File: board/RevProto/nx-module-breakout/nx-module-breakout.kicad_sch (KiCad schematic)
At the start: 20 parts, among them J1 Conn_02x15_Odd_Even, J2 DF40C-60DS-0.4V(51), J3 Conn_02x15_Odd_Even, J4 Conn_02x15_Odd_Even, J5 DF40C-60DS-0.4V(51), J6 SFV22R-2STE1HLF, J7 SFV22R-2STE1HLF, J8 Conn_02x06_Odd_Even

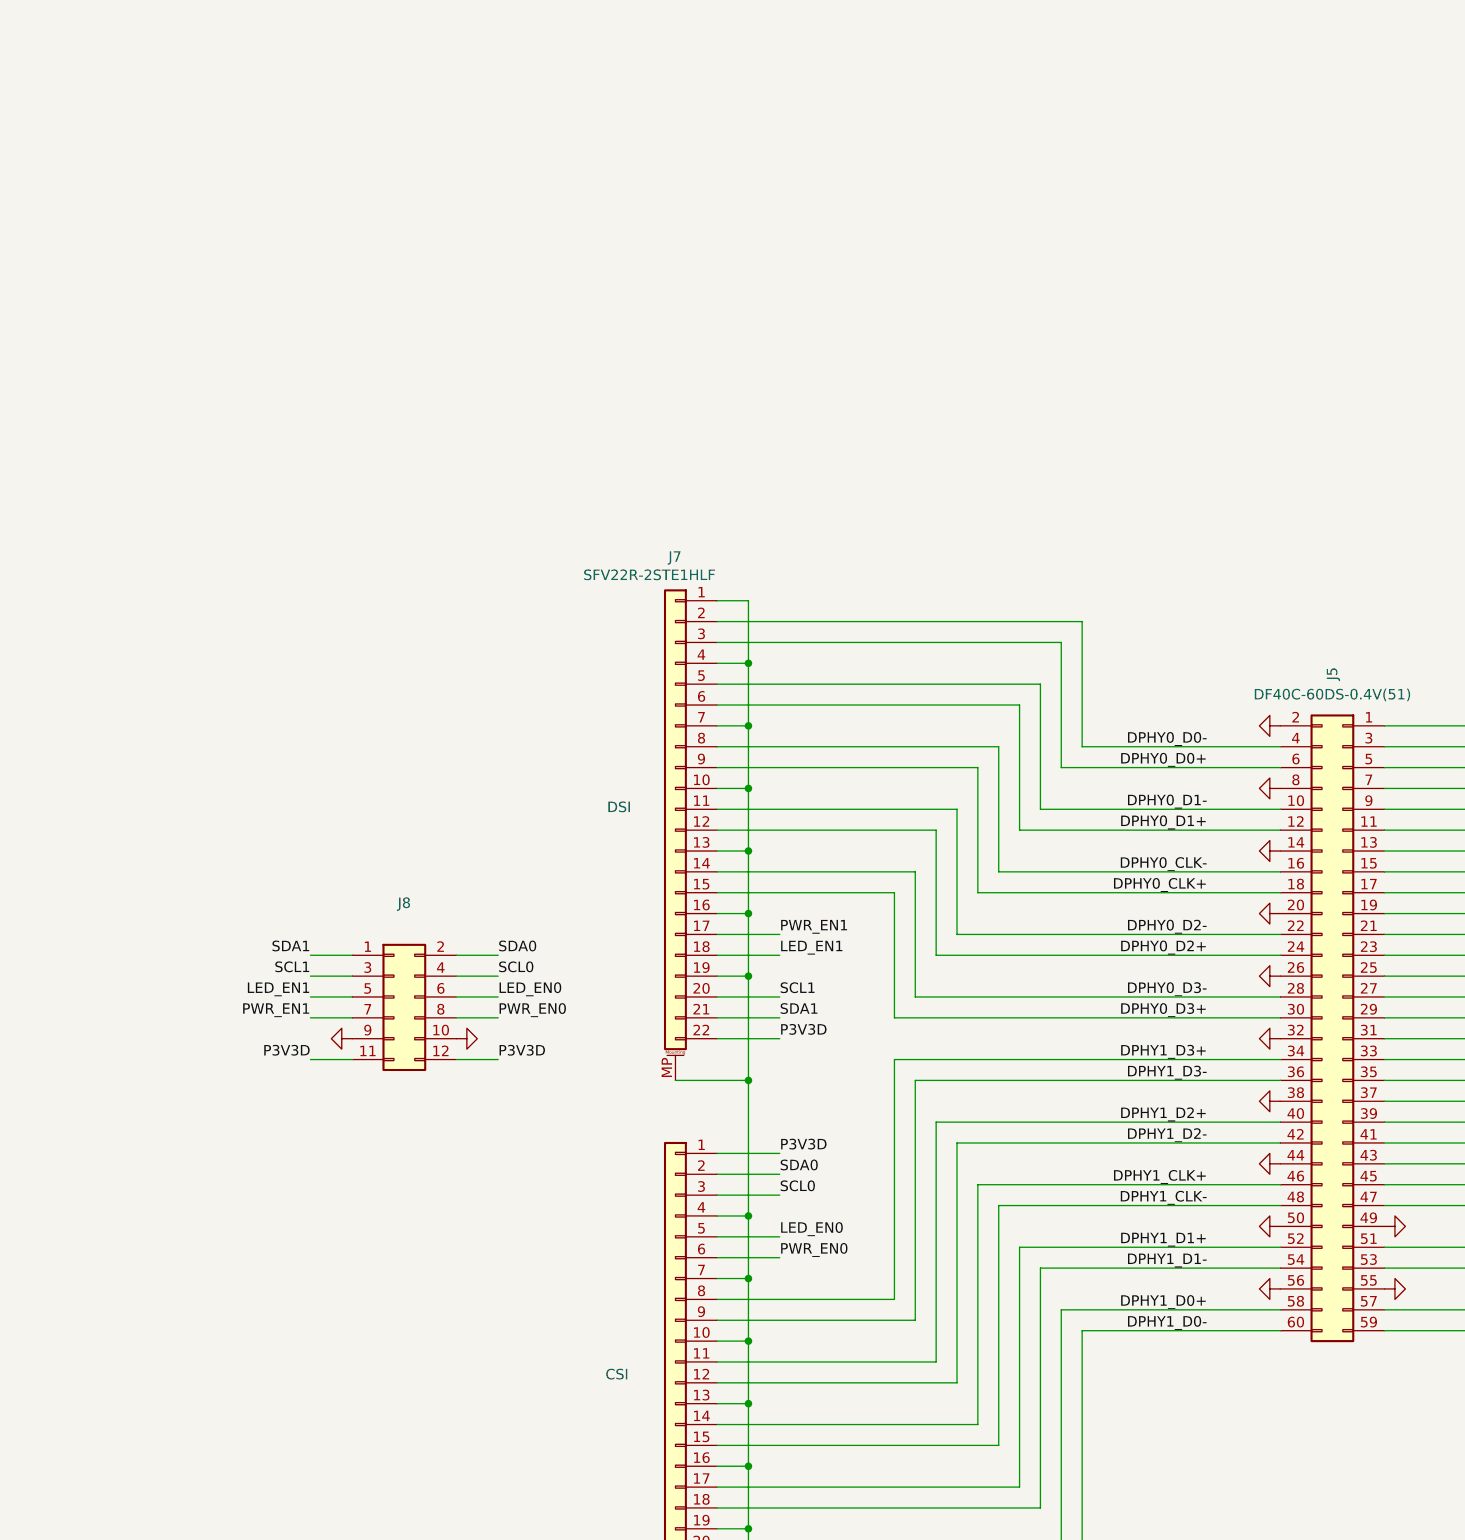
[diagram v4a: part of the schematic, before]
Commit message: Add USB connector, LDOs for power.
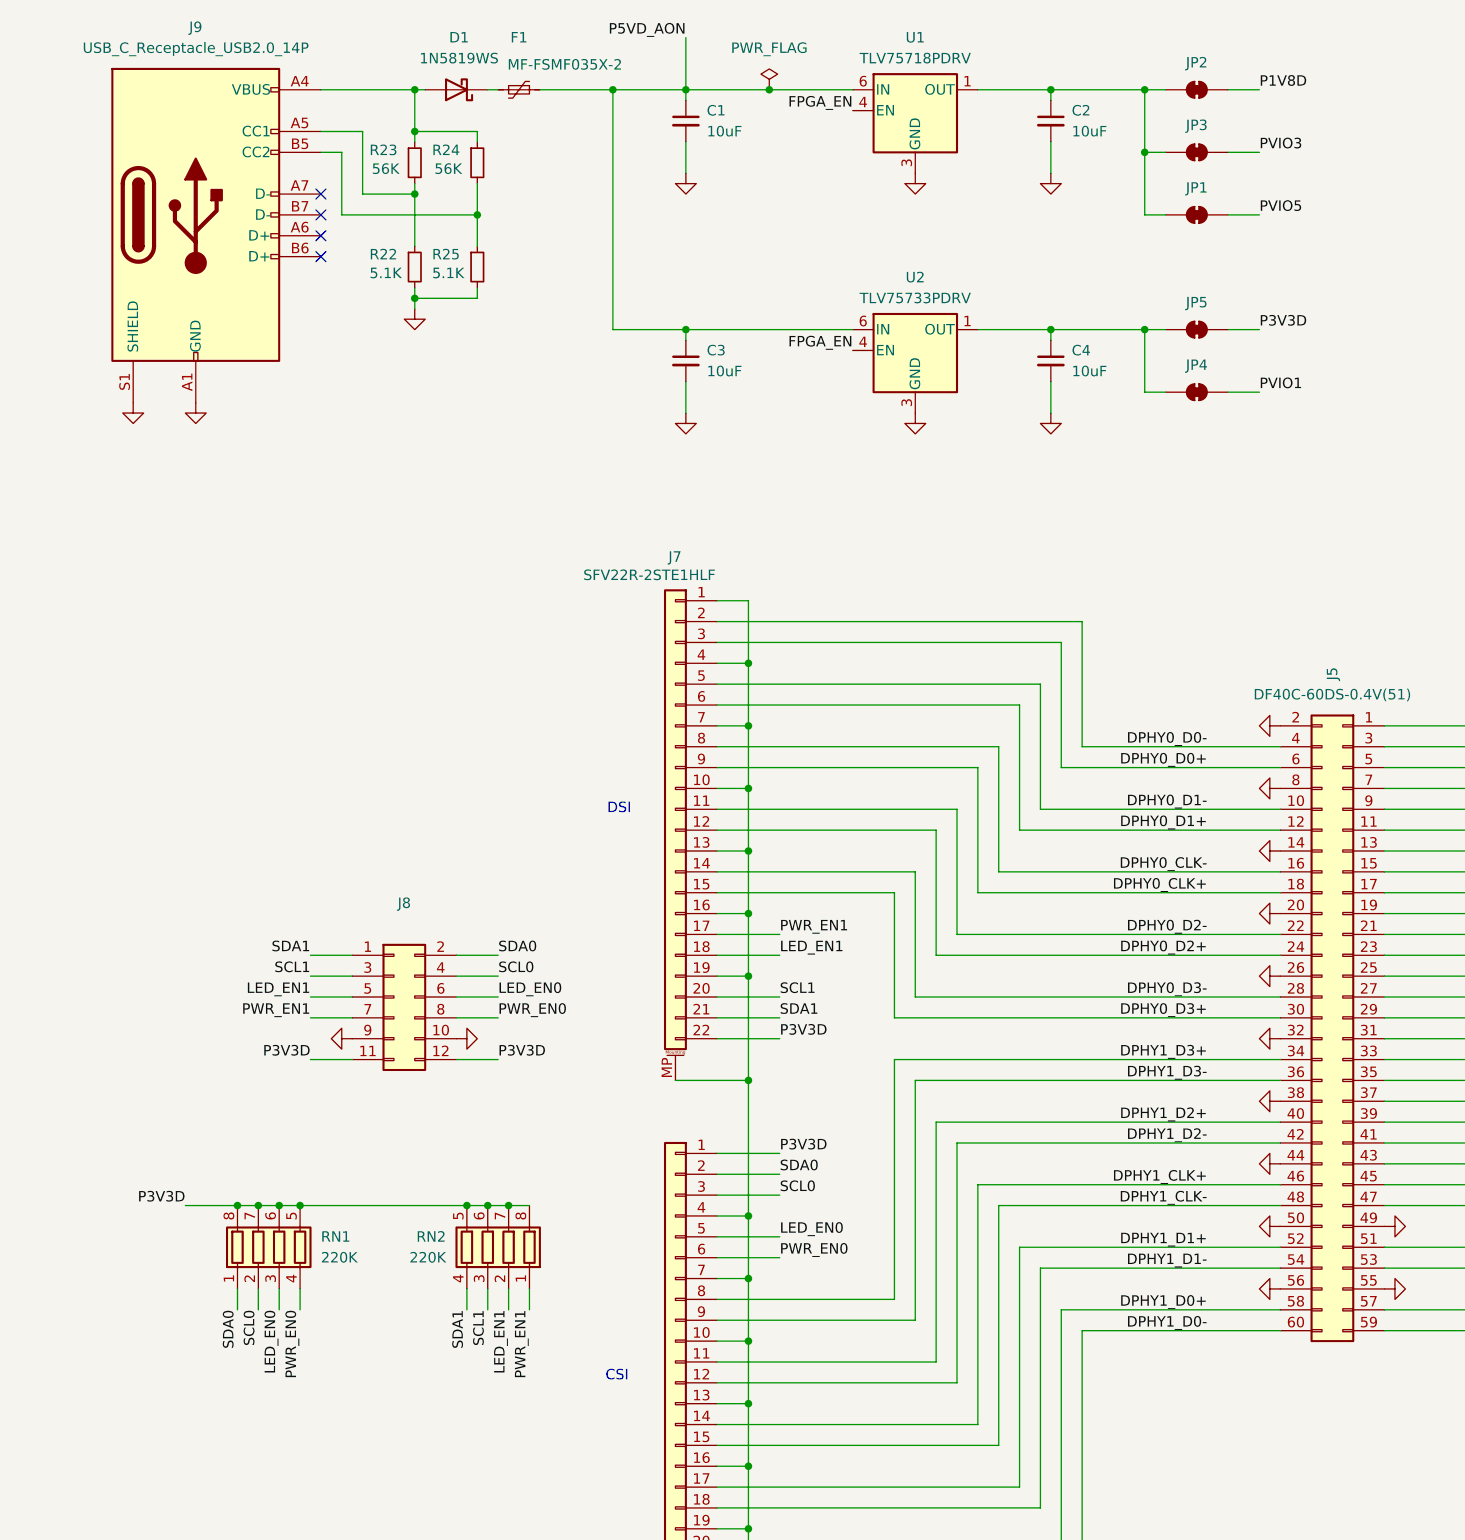
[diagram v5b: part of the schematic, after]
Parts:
- added C1, C2, C3, C4: 10uF, Capacitor_SMD:C_0402_1005Metric, symbol Device:C_Small
- added D1: 1N5819WS, Diode_SMD:D_SOD-323, symbol Diode:1N5817
- added F1: MF-FSMF035X-2, Resistor_SMD:R_0201_0603Metric, symbol Device:Polyfuse_Small
- added J9: USB_C_Receptacle_USB2.0_14P, Connector_USB:USB_C_Receptacle_HRO_TYPE-C-31-M-12, symbol Connector:USB_C_Receptacle_USB2.0_14P
- added JP1, JP2, JP3, JP4, JP5: SolderJumper_2_Bridged, Jumper:SolderJumper-2_P1.3mm_Bridged_RoundedPad1.0x1.5mm, symbol Jumper:SolderJumper_2_Bridged
- added R22, R25: 5.1K, Resistor_SMD:R_0402_1005Metric, symbol Device:R_Small
- added R23, R24: 56K, Resistor_SMD:R_0402_1005Metric, symbol Device:R_Small
- added RN1, RN2: 220K, Resistor_SMD:R_Array_Convex_4x0402, symbol Device:R_Pack04
- added U1: TLV75718PDRV, Package_SON:WSON-6-1EP_2x2mm_P0.65mm_EP1x1.6mm, symbol Regulator_Linear:TLV75718PDRV
- added U2: TLV75733PDRV, Package_SON:WSON-6-1EP_2x2mm_P0.65mm_EP1x1.6mm, symbol Regulator_Linear:TLV75733PDRV
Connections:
- net FPGA_EN: now also U1.4 (EN), U2.4 (EN)
- net GND: now also C1.2, C2.2, C3.2, C4.2, J9.A1 (GND), J9.A12 (GND), J9.B1 (GND), J9.B12 (GND), J9.S1 (SHIELD), R22.2, R25.2, U1.3 (GND), U1.7 (GND), U2.3 (GND), U2.7 (GND)
- net LED_EN0: now also RN1.3 (R3.1)
- net LED_EN1: now also RN2.2 (R2.1)
- net P1V8D: now also JP2.2 (B)
- net P3V3D: now also JP5.2 (B), RN1.5 (R4.2), RN1.6 (R3.2), RN1.7 (R2.2), RN1.8 (R1.2), RN2.5 (R4.2), RN2.6 (R3.2), RN2.7 (R2.2), RN2.8 (R1.2)
- net P5VD_AON: now also C1.1, C3.1, F1.1, U1.6 (IN), U2.6 (IN)
- net PVIO1: now also JP4.2 (B)
- net PVIO3: now also JP3.2 (B)
- net PVIO5: now also JP1.2 (B)
- net PWR_EN0: now also RN1.4 (R4.1)
- net PWR_EN1: now also RN2.1 (R1.1)
- net SCL0: now also RN1.2 (R2.1)
- net SCL1: now also RN2.3 (R3.1)
- net SDA0: now also RN1.1 (R1.1)
- net SDA1: now also RN2.4 (R4.1)
- new net: J9.A5 (CC1), R22.1, R23.2
- new net: D1.2 (A), J9.A4 (VBUS), J9.A9 (VBUS), J9.B4 (VBUS), J9.B9 (VBUS), R23.1, R24.1
- new net: C2.1, JP1.1 (A), JP2.1 (A), JP3.1 (A), U1.1 (OUT)
- new net: D1.1 (K), F1.2
- new net: J9.B5 (CC2), R24.2, R25.1
- new net: C4.1, JP4.1 (A), JP5.1 (A), U2.1 (OUT)
- no-connect marks 5 -> 9

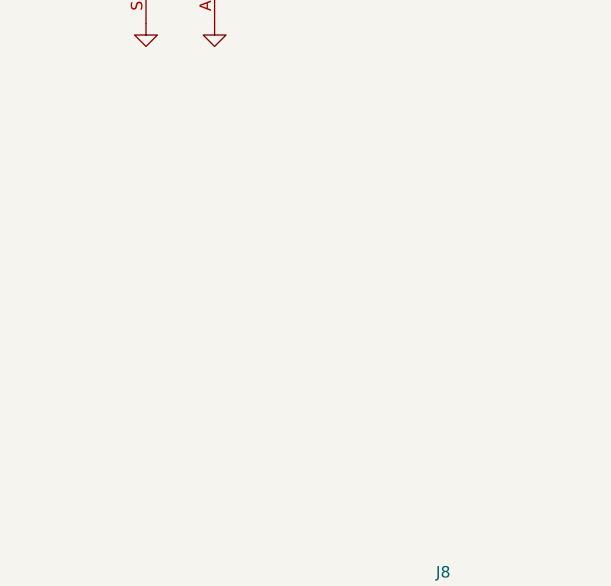
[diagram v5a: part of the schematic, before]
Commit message: Add power LED to breakout
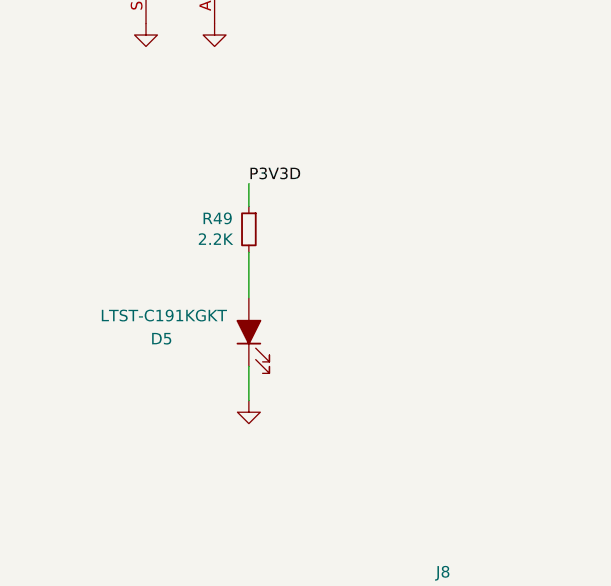
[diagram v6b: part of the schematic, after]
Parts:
- added D5: LTST-C191KGKT, LED_SMD:LED_0603_1608Metric, symbol UPduino_v3.0:Device_LED_ALT
- added R49: 2.2K, Resistor_SMD:R_0402_1005Metric, symbol Device:R_Small
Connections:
- net GND: now also D5.1 (K)
- net P3V3D: now also R49.1
- new net: D5.2 (A), R49.2

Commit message: Move breakout voltage regulators to leave space for header silk screen labels
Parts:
- F1: footprint Resistor_SMD:R_0201_0603Metric -> Resistor_SMD:R_0603_1608Metric
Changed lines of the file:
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@@
 			)
 		)
-		(property "Footprint" "Resistor_SMD:R_0201_0603Metric"
+		(property "Footprint" "Resistor_SMD:R_0603_1608Metric"
 			(at 80.01 34.29 0)
 			(effects

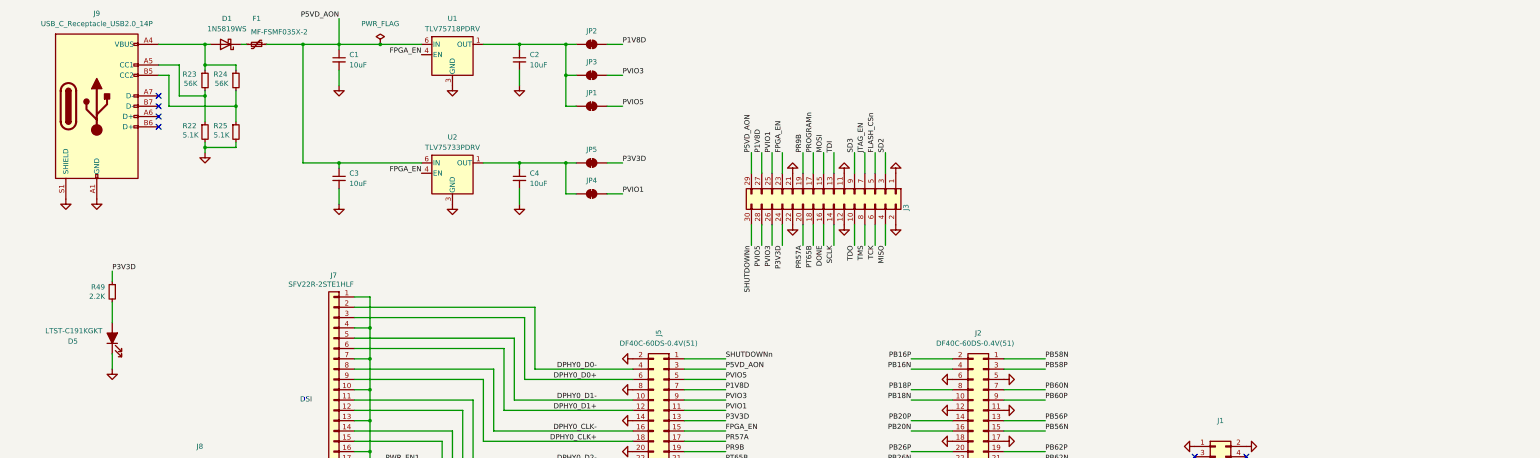
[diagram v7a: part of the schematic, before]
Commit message: Add JTAG connector to breakout board. Replace power LED with DONE LED. Plot schematic.
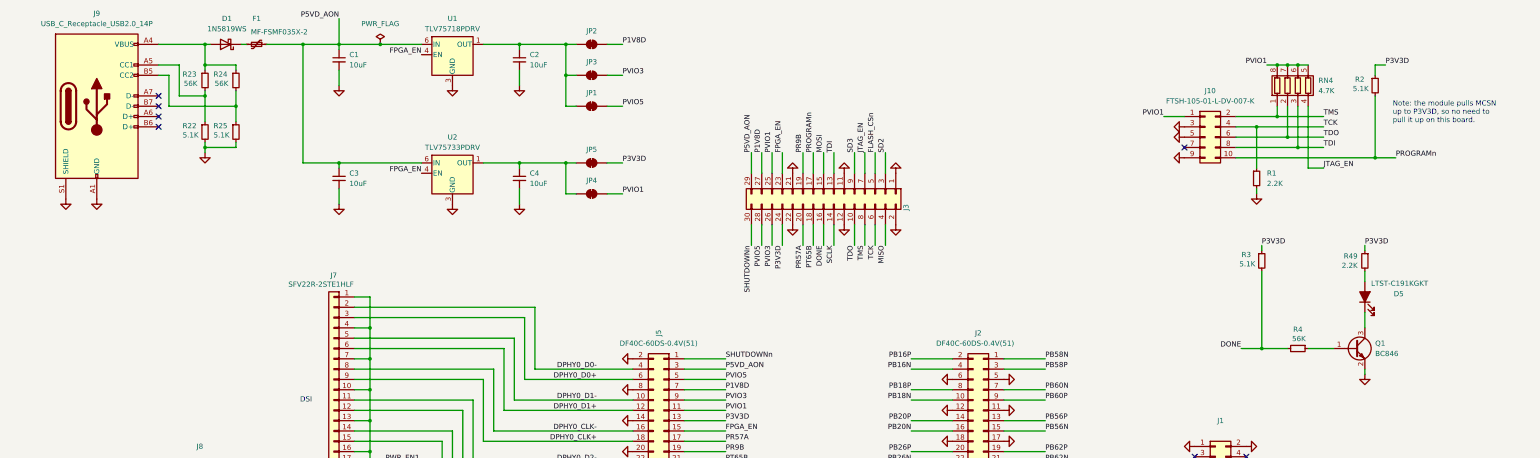
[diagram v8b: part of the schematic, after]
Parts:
- added J10: FTSH-105-01-L-DV-007-K, Connector_PinHeader_1.27mm:PinHeader_2x05_P1.27mm_Vertical_SMD, symbol Connector_Generic:Conn_02x05_Odd_Even
- added Q1: BC846, Package_TO_SOT_SMD:SOT-23, symbol Transistor_BJT:BC846
- added R1: 2.2K, Resistor_SMD:R_0402_1005Metric, symbol Device:R_Small
- added R2, R3: 5.1K, Resistor_SMD:R_0402_1005Metric, symbol Device:R_Small
- added R4: 56K, Resistor_SMD:R_0402_1005Metric, symbol Device:R_Small
- added RN4: 4.7K, Resistor_SMD:R_Array_Convex_4x0402, symbol Device:R_Pack04
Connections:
- net DONE: now also R3.2, R4.2
- net GND: now also J10.3 (Pin_3), J10.5 (Pin_5), J10.9 (Pin_9), Q1.2 (E), R1.2; no longer D5.1 (K)
- net JTAG_EN: now also RN4.4 (R4.1)
- net P3V3D: now also R2.1, R3.1
- net PROGRAMn: now also J10.10 (Pin_10), R2.2
- net PVIO1: now also J10.1 (Pin_1), RN4.5 (R4.2), RN4.6 (R3.2), RN4.7 (R2.2), RN4.8 (R1.2)
- net TCK: now also J10.4 (Pin_4), R1.1
- net TDI: now also J10.8 (Pin_8), RN4.3 (R3.1)
- net TDO: now also J10.6 (Pin_6), RN4.2 (R2.1)
- net TMS: now also J10.2 (Pin_2), RN4.1 (R1.1)
- new net: Q1.1 (B), R4.1
- new net: D5.1 (K), Q1.3 (C)
- no-connect marks 9 -> 10
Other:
- note added: "Note: the module pulls MCSN up to P3V3D, so no need to pull it up on this board."
- moved on the sheet: D5, R49
